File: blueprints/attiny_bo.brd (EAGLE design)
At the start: 35.8 x 20 mm, 9 parts, among them IC1 ATTiny85, IC4 LB1973M, J1 AVR_SPI_PRG_6NS

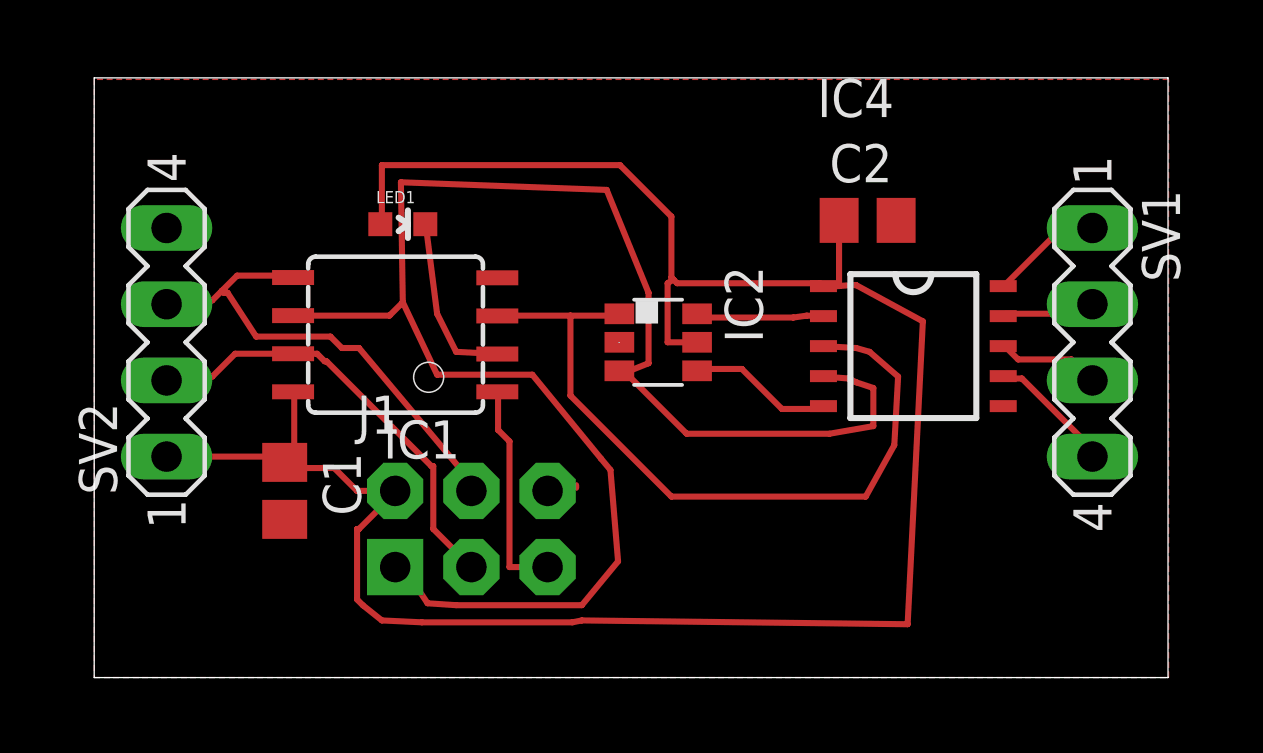
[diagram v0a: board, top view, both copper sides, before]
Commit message: simple breakout for attiny with ISP and 2x5 breakout header with pins in port order
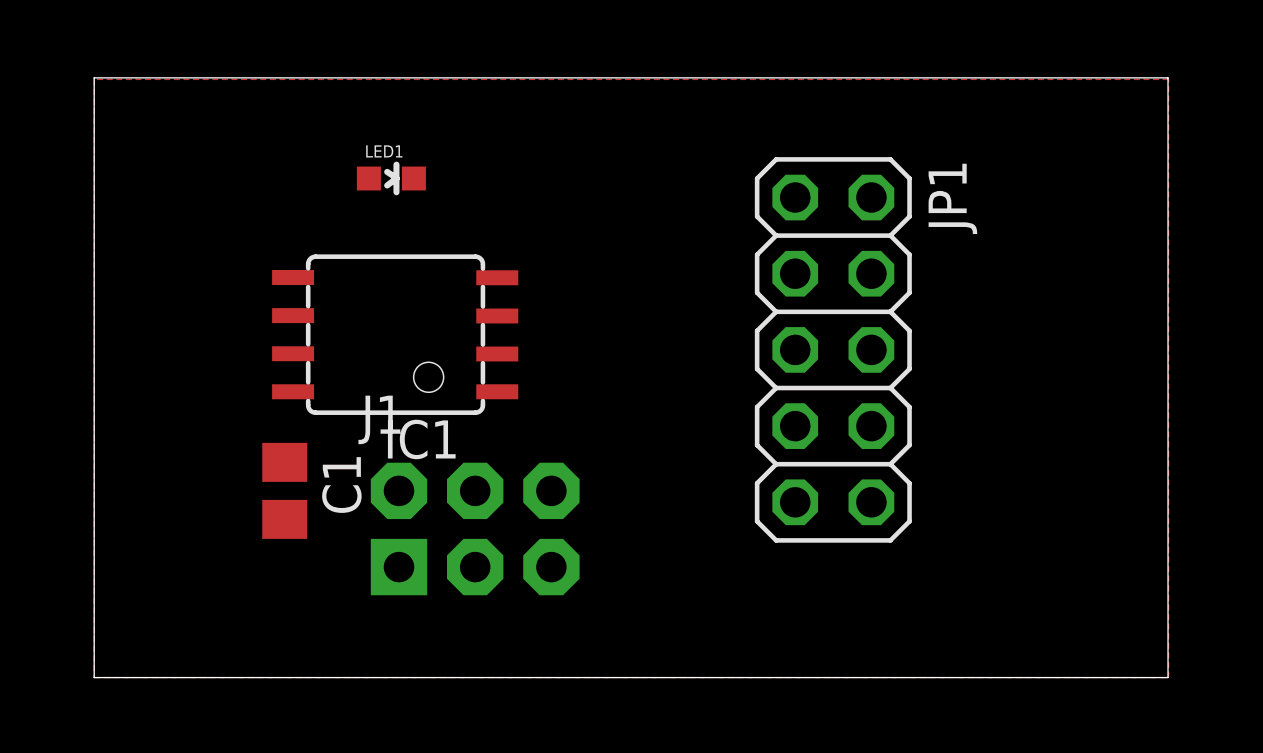
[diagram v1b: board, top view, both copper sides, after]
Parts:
- removed C2: (no value), rcl:C0805
- removed IC2: (no value), dp_devices:DBV-R-PDSO-G6
- removed IC4: LB1973M, LB1973M:SSOP10
- removed SV1, SV2: (no value), con-lstb:MA04-1
- added JP1: (no value), pinhead:2X05
- moved LED1 1.57 mm to (9.91, 16.6)
- moved J1 0.13 mm to (12.7, 4.95)
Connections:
- removed net IN2: IC2.4, IC4.5
- removed net N$2: IC2.6, IC4.2
- removed net OUT1: IC4.8, SV1.3
- removed net OUT2: IC4.7, SV1.4
- removed net OUT3: IC4.9, SV1.2
- removed net OUT4: IC4.10, SV1.1
- net +5V: now also JP1.10, JP1.9; no longer C2.1, IC2.5, IC4.1, SV2.1
- net GND: now also JP1.1, JP1.2; no longer C2.2, IC2.2, IC4.6, SV2.4
- net IN1/MISO: now also JP1.5; no longer IC2.3, IC4.4
- net N$1: now also JP1.6; no longer IC2.1, IC4.3
- net N$3: now also JP1.8
- net N$6: now also JP1.4
- net SCL/SCK: now also JP1.7; no longer SV2.2
- net SDA/MOSI: now also JP1.3; no longer SV2.3
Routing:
- net +5V: track 72.8 -> 0.00 mm
- net IN1/MISO: track 55.8 -> 0.00 mm
- net N$1: track 25.1 -> 0.00 mm
- net SDA/MOSI: track 16.6 -> 0.00 mm
- net SCL/SCK: track 14.7 -> 0.00 mm
- net N$6: track 7.29 -> 0.00 mm
- net N$3: track 5.82 -> 0.00 mm
- net IN2: track 4.84 -> 0.00 mm
- net N$2: track 4.28 -> 0.00 mm
- net OUT2: track 4.23 -> 0.00 mm
- net OUT4: track 3.77 -> 0.00 mm
- net OUT1: track 3.45 -> 0.00 mm
- net OUT3: track 3.13 -> 0.00 mm
- net GND: track 2.58 -> 0.00 mm

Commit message: put the grounds between signals in the 5x2 header
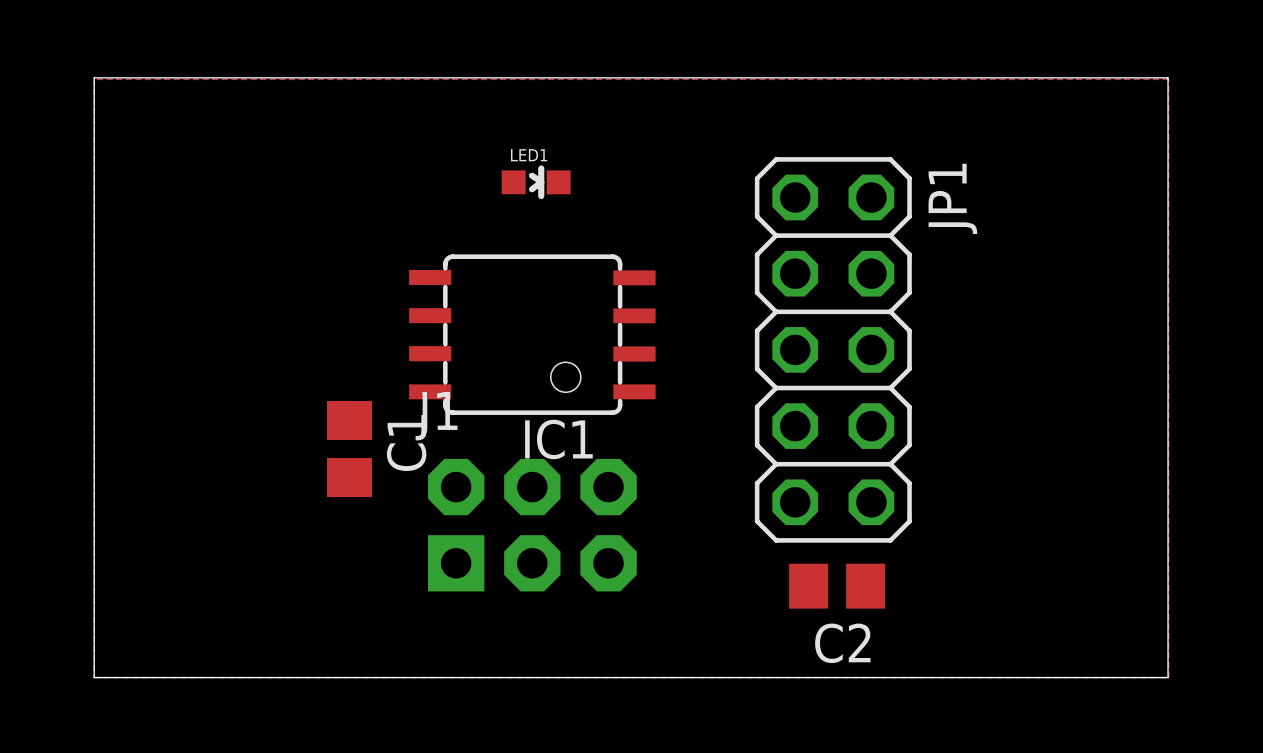
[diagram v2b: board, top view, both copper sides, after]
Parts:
- added C2: (no value), rcl:C0805
- moved LED1 4.83 mm to (14.7, 16.5)
- moved IC1 4.57 mm to (14.6, 11.4)
- moved C1 2.57 mm to (8.51, 7.62)
- moved J1 1.91 mm to (14.6, 5.08)
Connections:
- net +5V: now also C2.1; no longer JP1.9
- net GND: now also C2.2, JP1.4, JP1.7; no longer JP1.2
- net N$6: now also JP1.2; no longer JP1.4
- net SCL/SCK: now also JP1.9; no longer JP1.7
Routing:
- added copper zone on layer 16, net GND
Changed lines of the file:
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@@
 <layer number="14" name="Route14" color="1" fill="6" visible="no" active="no"/>
 <layer number="15" name="Route15" color="4" fill="6" visible="no" active="no"/>
-<layer number="16" name="Bottom" color="1" fill="1" visible="no" active="no"/>
+<layer number="16" name="Bottom" color="1" fill="1" visible="yes" active="yes"/>
 <layer number="17" name="Pads" color="2" fill="1" visible="yes" active="yes"/>
 <layer number="18" name="Vias" color="2" fill="1" visible="yes" active="yes"/>
@@
 necessary adjustments and save your customized
 design rules under a new name.</description>
-<param name="layerSetup" value="1"/>
+<param name="layerSetup" value="1*16"/>
 <param name="mtCopper" value="0.035mm 0.035mm 0.035mm 0.035mm 0.035mm 0.035mm 0.035mm 0.035mm 0.035mm 0.035mm 0.035mm 0.035mm 0.035mm 0.035mm 0.035mm 0.035mm"/>
 <param name="mtIsolate" value="1.5mm 0.15mm 0.2mm 0.15mm 0.2mm 0.15mm 0.2mm 0.15mm 0.2mm 0.15mm 0.2mm 0.15mm 0.2mm 0.15mm 0.2mm"/>
@@
 </autorouter>
 <elements>
-<element name="IC1" library="atmel" package="8S2" value="ATTiny85" x="10.033" y="11.43" rot="R90">
-<attribute name="OC_NEWARK" value="96K6522" x="15.113" y="38.1" size="1.778" layer="27" rot="R90" display="off"/>
-<attribute name="MPN" value="ATTINY13-20SU" x="15.113" y="38.1" size="1.778" layer="27" rot="R90" display="off"/>
-<attribute name="MF" value="" x="15.113" y="38.1" size="1.778" layer="27" rot="R90" display="off"/>
-<attribute name="OC_FARNELL" value="9171568" x="15.113" y="38.1" size="1.778" layer="27" rot="R90" display="off"/>
+<element name="IC1" library="atmel" package="8S2" value="ATTiny85" x="14.605" y="11.43" rot="R90">
+<attribute name="OC_NEWARK" value="96K6522" x="19.685" y="38.1" size="1.778" layer="27" rot="R90" display="off"/>
+<attribute name="MPN" value="ATTINY13-20SU" x="19.685" y="38.1" size="1.778" layer="27" rot="R90" display="off"/>
+<attribute name="MF" value="" x="19.685" y="38.1" size="1.778" layer="27" rot="R90" display="off"/>
+<attribute name="OC_FARNELL" value="9171568" x="19.685" y="38.1" size="1.778" layer="27" rot="R90" display="off"/>
 </element>
-<element name="J1" library="SparkFun-Connectors" package="2X3-NS" value="AVR_SPI_PRG_6NS" x="12.7" y="4.953"/>
-<element name="C1" library="rcl" package="C0805" value="" x="6.35" y="6.223" rot="R270"/>
-<element name="LED1" library="SparkFun-LED" package="LED-0603" value="" x="9.906" y="16.637" rot="R270"/>
+<element name="J1" library="SparkFun-Connectors" package="2X3-NS" value="AVR_SPI_PRG_6NS" x="14.605" y="5.08"/>
+<element name="C1" library="rcl" package="C0805" value="" x="8.509" y="7.62" rot="R270"/>
+<element name="LED1" library="SparkFun-LED" package="LED-0603" value="" x="14.732" y="16.51" rot="R270"/>
 <element name="JP1" library="pinhead" package="2X05" value="" x="24.638" y="10.922" rot="R270"/>
+<element name="C2" library="rcl" package="C0805" value="" x="24.765" y="3.048" rot="R180"/>
 </elements>
 <signals>
@@
 <contactref element="J1" pad="1"/>
 <contactref element="JP1" pad="5"/>
-<wire x1="10.16" y1="3.683" x2="23.368" y2="10.922" width="0" layer="19" extent="1-1"/>
-<wire x1="6.629" y1="12.065" x2="10.16" y2="3.683" width="0" layer="19" extent="1-1"/>
+<wire x1="11.201" y1="12.065" x2="23.368" y2="10.922" width="0" layer="19" extent="1-1"/>
+<wire x1="12.065" y1="3.81" x2="11.201" y2="12.065" width="0" layer="19" extent="1-1"/>
 </signal>
 <signal name="GND">
@@
 <contactref element="C1" pad="2"/>
 <contactref element="JP1" pad="1"/>
-<contactref element="JP1" pad="2"/>
+<contactref element="JP1" pad="4"/>
+<contactref element="JP1" pad="7"/>
+<contactref element="C2" pad="2"/>
+<polygon width="0.2032" layer="16" isolate="0.4064">
+<vertex x="0" y="19.939"/>
+<vertex x="0" y="0"/>
+<vertex x="35.814" y="0"/>
+<vertex x="35.814" y="19.939"/>
+</polygon>
 </signal>
 <signal name="+5V">
@@
 <contactref element="C1" pad="1"/>
 <contactref element="LED1" pad="A"/>
-<contactref element="JP1" pad="9"/>
 <contactref element="JP1" pad="10"/>
-<wire x1="23.368" y1="5.842" x2="25.908" y2="5.842" width="0" layer="19" extent="1-1"/>
-<wire x1="10.16" y1="6.223" x2="23.368" y2="5.842" width="0" layer="19" extent="1-1"/>
-<wire x1="6.35" y1="7.173" x2="10.16" y2="6.223" width="0" layer="19" extent="1-1"/>
-<wire x1="6.629" y1="9.525" x2="6.35" y2="7.173" width="0" layer="19" extent="1-1"/>
-<wire x1="9.156" y1="16.637" x2="6.629" y2="9.525" width="0" layer="19" extent="1-1"/>
+<contactref element="C2" pad="1"/>
+<wire x1="25.715" y1="3.048" x2="25.908" y2="5.842" width="0" layer="19" extent="1-1"/>
+<wire x1="12.065" y1="6.35" x2="25.908" y2="5.842" width="0" layer="19" extent="1-1"/>
+<wire x1="11.201" y1="9.525" x2="12.065" y2="6.35" width="0" layer="19" extent="1-1"/>
+<wire x1="8.509" y1="8.57" x2="11.201" y2="9.525" width="0" layer="19" extent="1-1"/>
+<wire x1="13.982" y1="16.51" x2="11.201" y2="9.525" width="0" layer="19" extent="1-1"/>
 </signal>
 <signal name="SDA/MOSI">
@@
 <contactref element="J1" pad="4"/>
 <contactref element="JP1" pad="3"/>
-<wire x1="12.7" y1="6.223" x2="23.368" y2="13.462" width="0" layer="19" extent="1-1"/>
-<wire x1="6.629" y1="13.335" x2="12.7" y2="6.223" width="0" layer="19" extent="1-1"/>
+<wire x1="14.605" y1="6.35" x2="23.368" y2="13.462" width="0" layer="19" extent="1-1"/>
+<wire x1="11.201" y1="13.335" x2="14.605" y2="6.35" width="0" layer="19" extent="1-1"/>
 </signal>
 <signal name="N$6">
 <contactref element="IC1" pad="1"/>
 <contactref element="J1" pad="5"/>
-<contactref element="JP1" pad="4"/>
-<wire x1="13.437" y1="9.525" x2="25.908" y2="13.462" width="0" layer="19" extent="1-1"/>
-<wire x1="15.24" y1="3.683" x2="13.437" y2="9.525" width="0" layer="19" extent="1-1"/>
+<contactref element="JP1" pad="2"/>
+<wire x1="18.009" y1="9.525" x2="25.908" y2="16.002" width="0" layer="19" extent="1-1"/>
+<wire x1="17.145" y1="3.81" x2="18.009" y2="9.525" width="0" layer="19" extent="1-1"/>
 </signal>
 <signal name="SCL/SCK">
 <contactref element="IC1" pad="7"/>
 <contactref element="J1" pad="3"/>
-<contactref element="JP1" pad="7"/>
-<wire x1="12.7" y1="3.683" x2="23.368" y2="8.382" width="0" layer="19" extent="1-1"/>
-<wire x1="6.629" y1="10.795" x2="12.7" y2="3.683" width="0" layer="19" extent="1-1"/>
+<contactref element="JP1" pad="9"/>
+<wire x1="14.605" y1="3.81" x2="23.368" y2="5.842" width="0" layer="19" extent="1-1"/>
+<wire x1="11.201" y1="10.795" x2="14.605" y2="3.81" width="0" layer="19" extent="1-1"/>
 </signal>
 <signal name="N$3">
@@
 <contactref element="IC1" pad="2"/>
 <contactref element="JP1" pad="8"/>
-<wire x1="13.437" y1="10.785" x2="25.908" y2="8.382" width="0" layer="19" extent="1-1"/>
-<wire x1="10.656" y1="16.637" x2="13.437" y2="10.785" width="0" layer="19" extent="1-1"/>
+<wire x1="18.009" y1="10.785" x2="25.908" y2="8.382" width="0" layer="19" extent="1-1"/>
+<wire x1="15.482" y1="16.51" x2="18.009" y2="10.785" width="0" layer="19" extent="1-1"/>
 </signal>
 <signal name="N$1">
 <contactref element="IC1" pad="3"/>
 <contactref element="JP1" pad="6"/>
-<wire x1="13.437" y1="12.055" x2="25.908" y2="10.922" width="0" layer="19" extent="1-1"/>
+<wire x1="18.009" y1="12.055" x2="25.908" y2="10.922" width="0" layer="19" extent="1-1"/>
 </signal>
 </signals>

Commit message: first autorouted version, board can be made smaller and needs some mounting holes etc
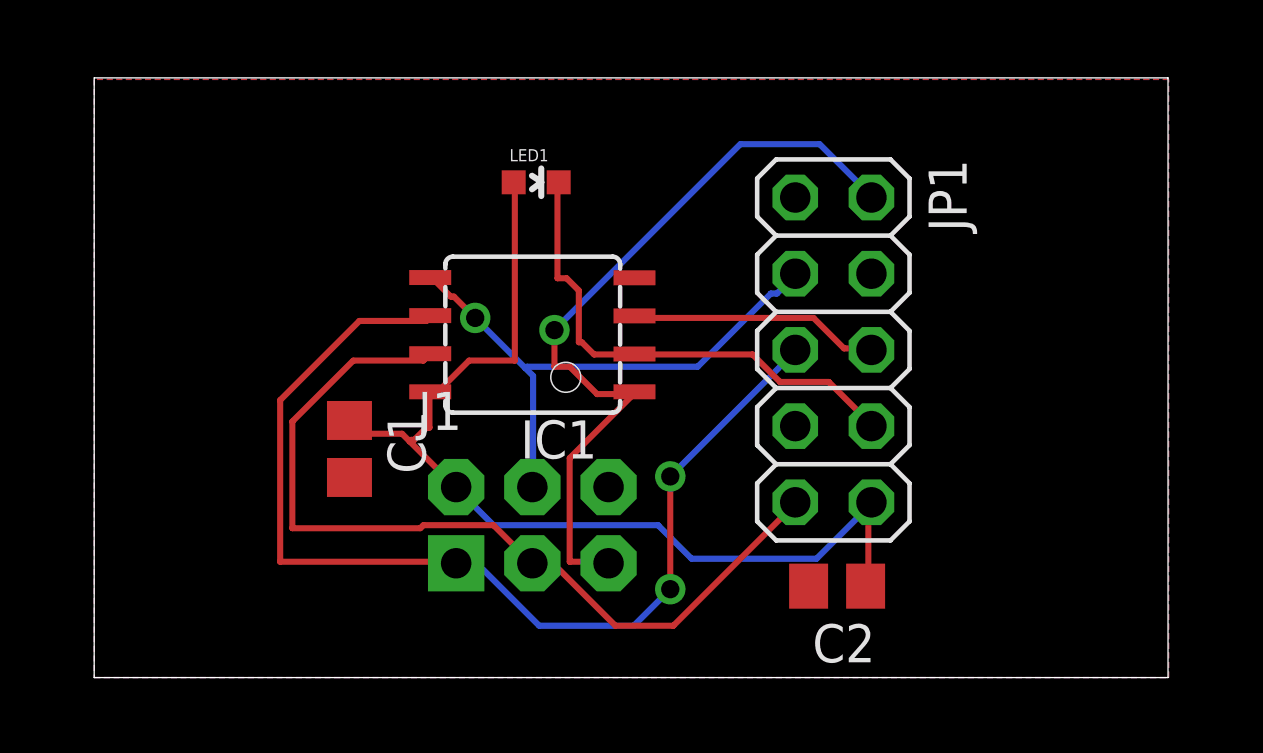
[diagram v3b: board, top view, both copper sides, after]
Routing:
- net IN1/MISO: track 0.00 -> 35.7 mm, vias 0 -> 2
- net +5V: track 0.00 -> 34.4 mm
- net SCL/SCK: track 0.00 -> 29.0 mm
- net N$6: track 0.00 -> 26.0 mm, vias 0 -> 1
- net SDA/MOSI: track 0.00 -> 18.8 mm, vias 0 -> 1
- net N$3: track 0.00 -> 16.8 mm
- net N$1: track 0.00 -> 8.40 mm

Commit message: use wider traces for 5v and gnd
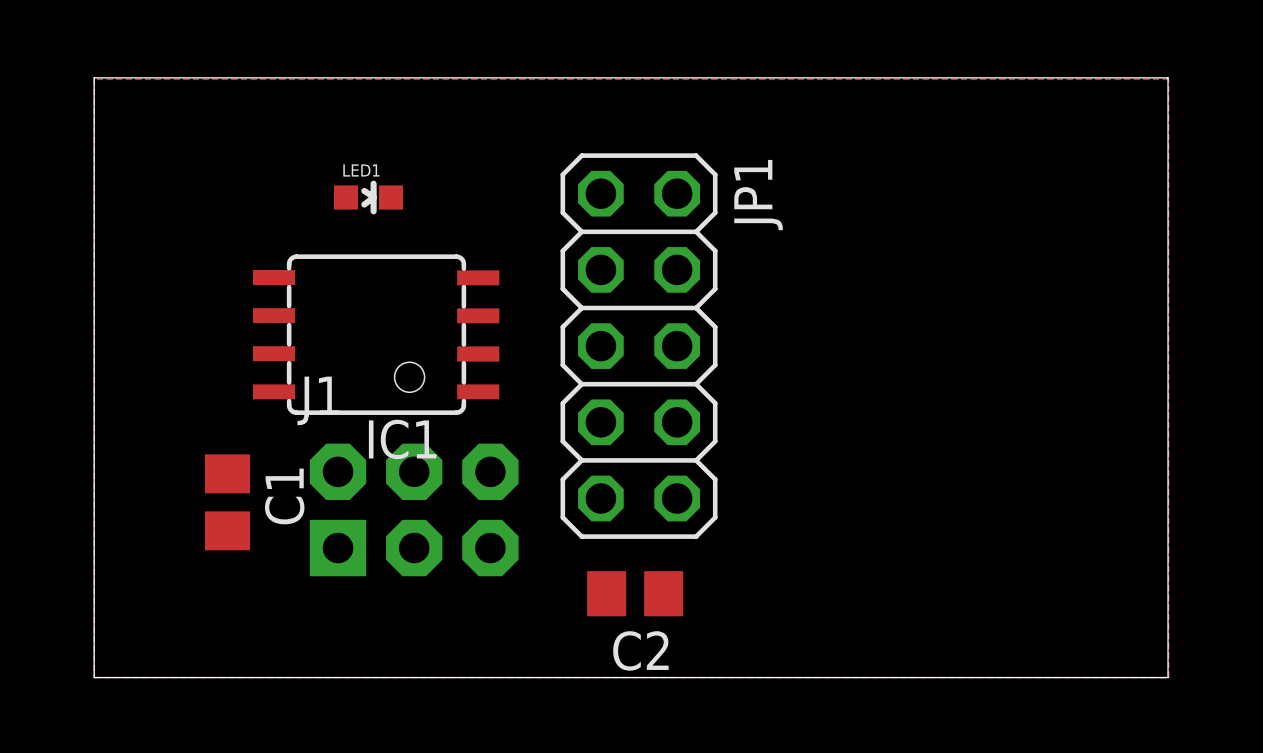
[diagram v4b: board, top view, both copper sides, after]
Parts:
- moved C2 6.74 mm to (18.0, 2.79)
- moved JP1 6.48 mm to (18.2, 11.0)
- moved LED1 5.61 mm to (9.14, 16.0)
- moved IC1 5.21 mm to (9.40, 11.4)
- moved C1 4.44 mm to (4.45, 5.84)
- moved J1 3.97 mm to (10.7, 5.59)
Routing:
- net IN1/MISO: track 35.7 -> 0.00 mm, vias 2 -> 0
- net +5V: track 34.4 -> 0.00 mm
- net SCL/SCK: track 29.0 -> 0.00 mm
- net N$6: track 26.0 -> 0.00 mm, vias 1 -> 0
- net SDA/MOSI: track 18.8 -> 0.00 mm, vias 1 -> 0
- net N$3: track 16.8 -> 0.00 mm
- net N$1: track 8.40 -> 0.00 mm

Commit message: mounting pads with GND access
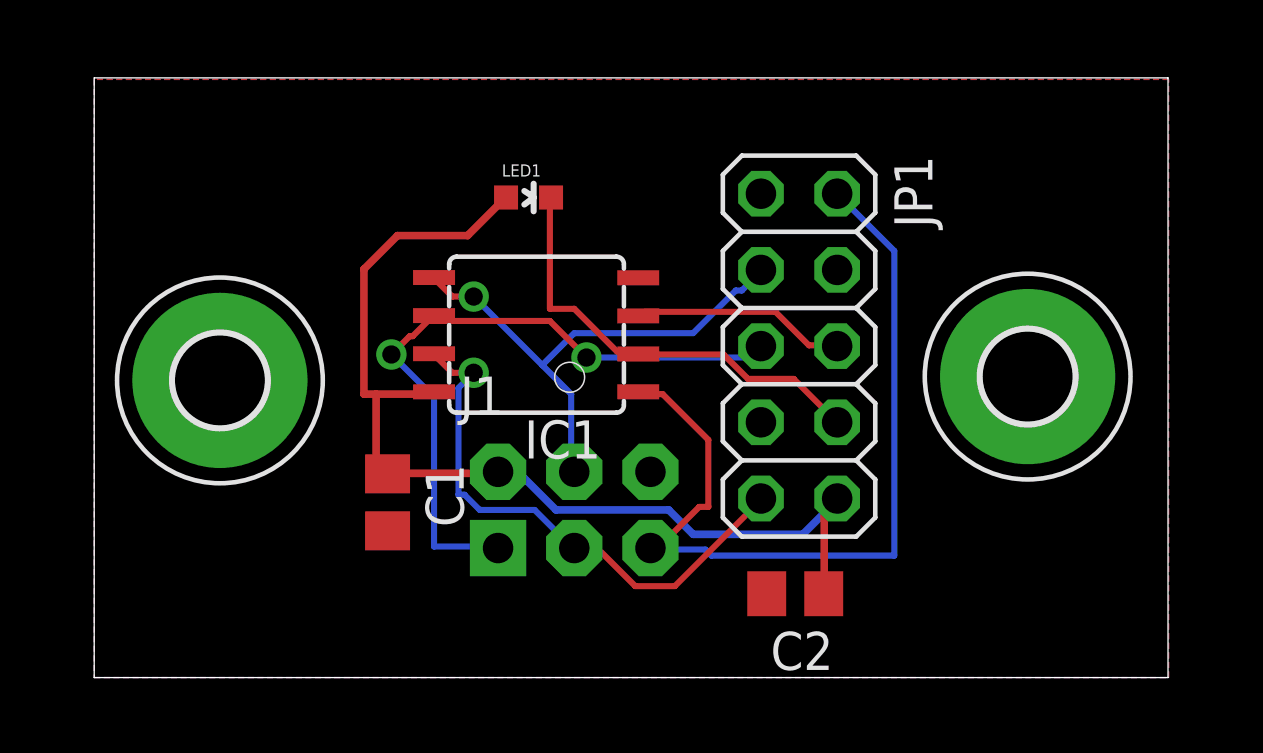
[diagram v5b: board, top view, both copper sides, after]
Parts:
- added H1, H2: MOUNT-PAD-ROUND3.0, holes:3,0-PAD
- moved C1 5.33 mm to (9.78, 5.84)
- moved C2 5.33 mm to (23.4, 2.79)
- moved IC1 5.33 mm to (14.7, 11.4)
- moved J1 5.33 mm to (16.0, 5.59)
- moved JP1 5.33 mm to (23.5, 11.0)
- moved LED1 5.33 mm to (14.5, 16.0)
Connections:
- net GND: now also H1.B3,0, H2.B3,0
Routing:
- net +5V: track 0.00 -> 35.4 mm
- net N$6: track 0.00 -> 28.9 mm
- net IN1/MISO: track 0.00 -> 23.0 mm, vias 0 -> 2
- net SCL/SCK: track 0.00 -> 18.5 mm, vias 0 -> 1
- net SDA/MOSI: track 0.00 -> 17.5 mm, vias 0 -> 1
- net N$3: track 0.00 -> 14.9 mm
- net N$1: track 0.00 -> 7.15 mm
